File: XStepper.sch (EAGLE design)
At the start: 74 parts, among them Q2 16 MHZ

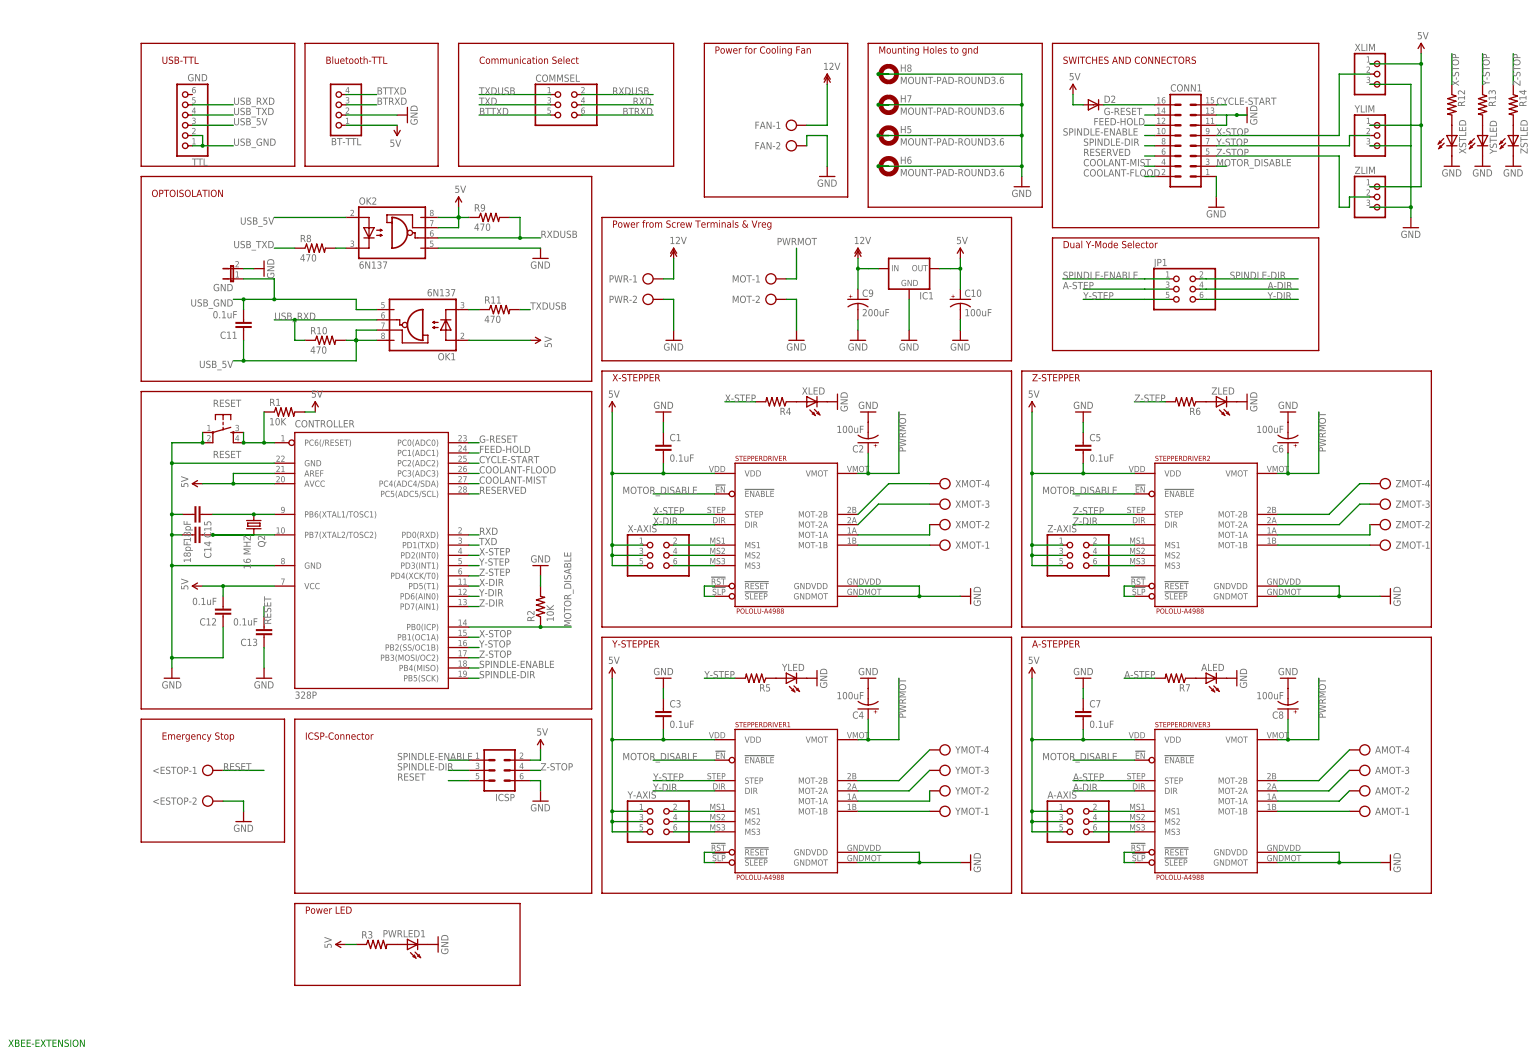
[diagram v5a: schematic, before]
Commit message: - add VMOT sign to driver for users
- remove circle for pod cuz they are different on drivers
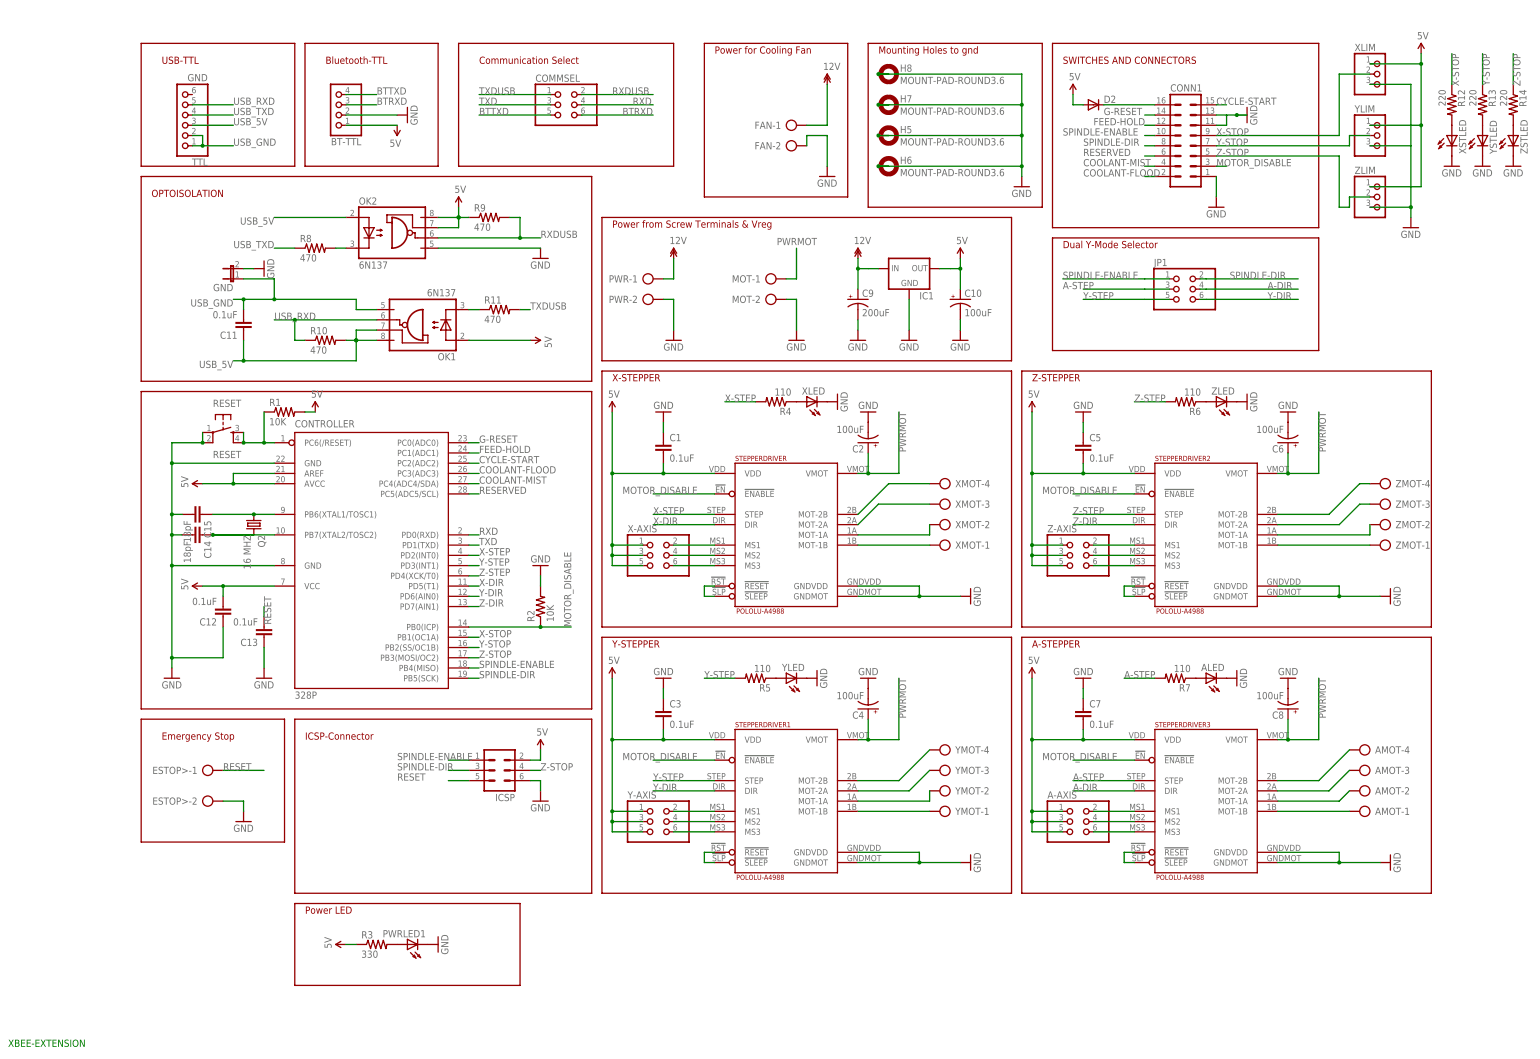
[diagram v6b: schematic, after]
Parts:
- R12, R13, R14: value (none) -> 220
- R3: value (none) -> 330
- R4, R5, R6, R7: value (none) -> 110
- renumbered <ESTOP to ESTOP>
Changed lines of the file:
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@@
 <?xml version="1.0" encoding="utf-8"?>
 <!DOCTYPE eagle SYSTEM "eagle.dtd">
-<eagle version="6.4">
+<eagle version="6.3">
 <drawing>
 <settings>
@@
 </variantdefs>
 <classes>
-<class number="0" name="default" width="0.3048" drill="0">
+<class number="0" name="default" width="0.2032" drill="0">
 <clearance class="0" value="0.2032"/>
 </class>
@@
 <part name="JP1" library="pinhead" deviceset="PINHD-2X3" device=""/>
 <part name="IC1" library="SparkFun-PowerIC" deviceset="V_REG_78XX" device="SINK"/>
-<part name="R3" library="SparkFun-Resistors" deviceset="RESISTOR" device="AXIAL-0.3"/>
+<part name="R3" library="SparkFun-Resistors" deviceset="RESISTOR" device="AXIAL-0.3" value="330"/>
 <part name="R8" library="SparkFun-Resistors" deviceset="RESISTOR" device="AXIAL-0.3" value="470"/>
 <part name="R9" library="SparkFun-Resistors" deviceset="RESISTOR" device="AXIAL-0.3" value="470"/>
@@
 <part name="R1" library="SparkFun-Resistors" deviceset="RESISTOR" device="AXIAL-0.3" value="10K"/>
 <part name="R2" library="SparkFun-Resistors" deviceset="RESISTOR" device="AXIAL-0.3" value="10K"/>
-<part name="R4" library="SparkFun-Resistors" deviceset="RESISTOR" device="AXIAL-0.3"/>
-<part name="R5" library="SparkFun-Resistors" deviceset="RESISTOR" device="AXIAL-0.3"/>
-<part name="R6" library="SparkFun-Resistors" deviceset="RESISTOR" device="AXIAL-0.3"/>
-<part name="R7" library="SparkFun-Resistors" deviceset="RESISTOR" device="AXIAL-0.3"/>
-<part name="R12" library="SparkFun-Resistors" deviceset="RESISTOR" device="AXIAL-0.3"/>
-<part name="R13" library="SparkFun-Resistors" deviceset="RESISTOR" device="AXIAL-0.3"/>
-<part name="R14" library="SparkFun-Resistors" deviceset="RESISTOR" device="AXIAL-0.3"/>
-<part name="&lt;ESTOP" library="con-ptr500" deviceset="AK500/2" device=""/>
+<part name="R4" library="SparkFun-Resistors" deviceset="RESISTOR" device="AXIAL-0.3" value="110"/>
+<part name="R5" library="SparkFun-Resistors" deviceset="RESISTOR" device="AXIAL-0.3" value="110"/>
+<part name="R6" library="SparkFun-Resistors" deviceset="RESISTOR" device="AXIAL-0.3" value="110"/>
+<part name="R7" library="SparkFun-Resistors" deviceset="RESISTOR" device="AXIAL-0.3" value="110"/>
+<part name="R12" library="SparkFun-Resistors" deviceset="RESISTOR" device="AXIAL-0.3" value="220"/>
+<part name="R13" library="SparkFun-Resistors" deviceset="RESISTOR" device="AXIAL-0.3" value="220"/>
+<part name="R14" library="SparkFun-Resistors" deviceset="RESISTOR" device="AXIAL-0.3" value="220"/>
+<part name="ESTOP&gt;" library="con-ptr500" deviceset="AK500/2" device=""/>
 <part name="GND39" library="SparkFun" deviceset="GND" device=""/>
 <part name="COMMSEL" library="pinhead" deviceset="PINHD-2X3" device=""/>
@@
 <instance part="R13" gate="G$1" x="332.74" y="165.1" rot="R270"/>
 <instance part="R14" gate="G$1" x="340.36" y="165.1" rot="R270"/>
-<instance part="&lt;ESTOP" gate="-1" x="15.24" y="0"/>
-<instance part="&lt;ESTOP" gate="-2" x="15.24" y="-7.62"/>
+<instance part="ESTOP&gt;" gate="-1" x="15.24" y="0"/>
+<instance part="ESTOP&gt;" gate="-2" x="15.24" y="-7.62"/>
 <instance part="GND39" gate="1" x="25.4" y="-12.7"/>
 <instance part="COMMSEL" gate="A" x="104.14" y="165.1"/>
@@
 </segment>
 <segment>
-<pinref part="&lt;ESTOP" gate="-2" pin="KL"/>
+<pinref part="ESTOP&gt;" gate="-2" pin="KL"/>
 <wire x1="20.32" y1="-7.62" x2="25.4" y2="-7.62" width="0.1524" layer="91"/>
 <wire x1="25.4" y1="-7.62" x2="25.4" y2="-10.16" width="0.1524" layer="91"/>
@@
 </segment>
 <segment>
-<pinref part="&lt;ESTOP" gate="-1" pin="KL"/>
+<pinref part="ESTOP&gt;" gate="-1" pin="KL"/>
 <wire x1="20.32" y1="0" x2="25.4" y2="0" width="0.1524" layer="91"/>
 <wire x1="25.4" y1="0" x2="30.48" y2="0" width="0.1524" layer="91"/>

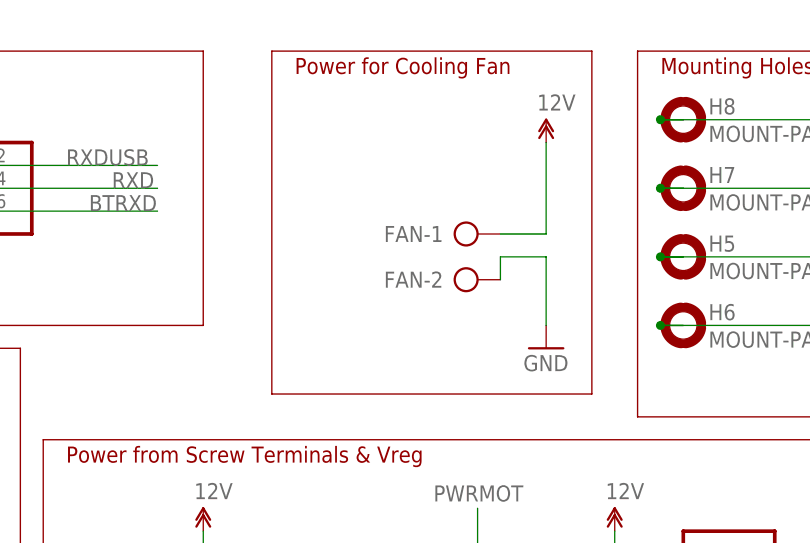
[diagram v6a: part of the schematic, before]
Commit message: - some changes for community
* move screw terminals for motors 1mm up for bigger caps
* add a 12V voltage regulator for fan
* replace powerled resitor to a small one
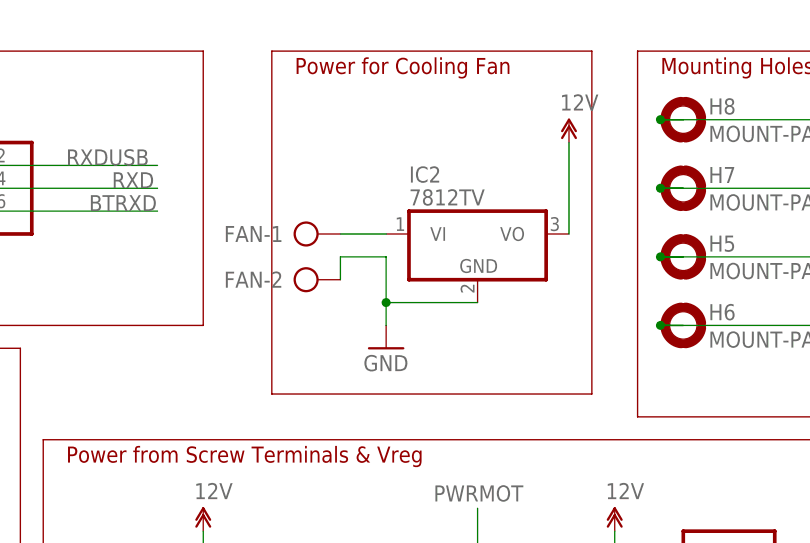
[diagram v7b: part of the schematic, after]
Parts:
- added IC2: 7812TV, linear:7812TV
- R3: device SparkFun-Resistors:RESISTORAXIAL-0.3 -> SparkFun-Resistors:RESISTORPTH-1/6W
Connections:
- new net N$46: FAN-1.KL, IC2.VI
- net 12V: now also IC2.VO; no longer FAN-1.KL
- net GND: now also IC2.GND
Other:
- moved on the sheet: FAN-1, FAN-2

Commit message: - bigger vmot caps 8mm
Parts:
- C2, C4, C6, C8: device resistor:CPOL-USE2.5-6 -> resistor:CPOL-USE3.5-8
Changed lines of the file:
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@@
 <part name="Y-AXIS" library="pinhead" deviceset="PINHD-2X3" device=""/>
 <part name="GND8" library="supply1" deviceset="GND" device=""/>
-<part name="C4" library="resistor" deviceset="CPOL-US" device="E2.5-6" value="100uF"/>
+<part name="C4" library="resistor" deviceset="CPOL-US" device="E3.5-8" value="100uF"/>
 <part name="GND9" library="supply1" deviceset="GND" device=""/>
 <part name="STEPPERDRIVER2" library="pololu-allegro" deviceset="POLOLU-ALLEGRO" device="" value="POLOLU-A4988"/>
@@
 <part name="Z-AXIS" library="pinhead" deviceset="PINHD-2X3" device=""/>
 <part name="GND11" library="supply1" deviceset="GND" device=""/>
-<part name="C6" library="resistor" deviceset="CPOL-US" device="E2.5-6" value="100uF"/>
+<part name="C6" library="resistor" deviceset="CPOL-US" device="E3.5-8" value="100uF"/>
 <part name="GND12" library="supply1" deviceset="GND" device=""/>
 <part name="U$26" library="SparkFun" deviceset="5V" device=""/>
@@
 <part name="A-AXIS" library="pinhead" deviceset="PINHD-2X3" device=""/>
 <part name="GND15" library="supply1" deviceset="GND" device=""/>
-<part name="C8" library="resistor" deviceset="CPOL-US" device="E2.5-6" value="100uF"/>
+<part name="C8" library="resistor" deviceset="CPOL-US" device="E3.5-8" value="100uF"/>
 <part name="GND16" library="supply1" deviceset="GND" device=""/>
 <part name="U$1" library="SparkFun" deviceset="5V" device=""/>
@@
 <part name="C5" library="resistor" deviceset="C-EU" device="025-025X050" value="0.1uF"/>
 <part name="C7" library="resistor" deviceset="C-EU" device="025-025X050" value="0.1uF"/>
-<part name="C2" library="resistor" deviceset="CPOL-US" device="E2.5-6" value="100uF"/>
+<part name="C2" library="resistor" deviceset="CPOL-US" device="E3.5-8" value="100uF"/>
 <part name="JP1" library="pinhead" deviceset="PINHD-2X3" device=""/>
 <part name="IC1" library="SparkFun-PowerIC" deviceset="V_REG_78XX" device="SINK"/>
